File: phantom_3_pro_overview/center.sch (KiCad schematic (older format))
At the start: 3 parts

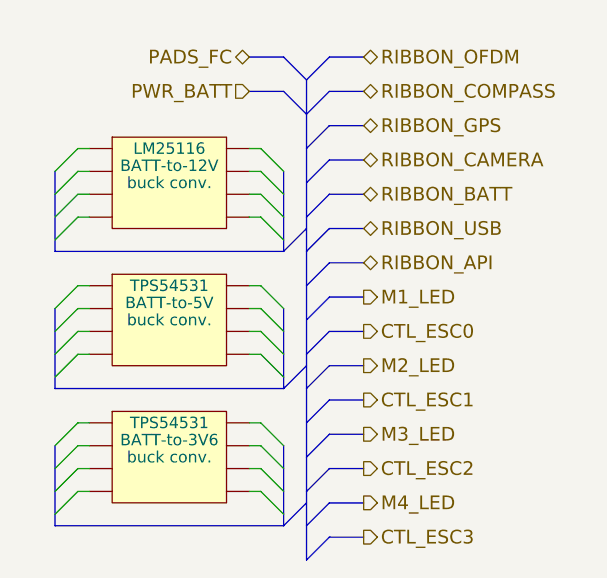
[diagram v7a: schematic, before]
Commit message: Overview: Separated gimbal power circuit.
This is to make sure the connection won't be interpreted as data link.
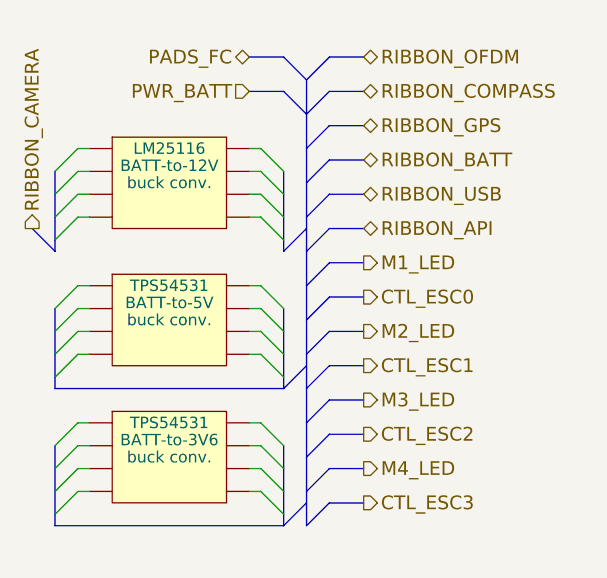
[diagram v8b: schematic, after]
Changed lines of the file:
@@
 $Descr User 5354 4725
 encoding utf-8
-Sheet 4 23
+Sheet 4 24
 Title "Overview of the Phantom 3 Pro Center part of MB"
 Date ""
@@
 Text HLabel 2950 1000 2    60   BiDi ~ 0
 RIBBON_GPS
+Text HLabel 1500 1450 1    60   Output ~ 0
+RIBBON_CAMERA
 Text HLabel 2950 1150 2    60   BiDi ~ 0
-RIBBON_CAMERA
+RIBBON_BATT
 Text HLabel 2950 1300 2    60   BiDi ~ 0
-RIBBON_BATT
+RIBBON_USB
 Text HLabel 2950 1450 2    60   BiDi ~ 0
-RIBBON_USB
-Text HLabel 2950 1600 2    60   BiDi ~ 0
 RIBBON_API
+Text HLabel 2950 1600 2    60   Output ~ 0
+M1_LED
 Text HLabel 2950 1750 2    60   Output ~ 0
-M1_LED
-Text HLabel 2950 1900 2    60   Output ~ 0
 CTL_ESC0
 Text HLabel 2450 850  0    60   Input ~ 0
 PWR_BATT
+Text HLabel 2950 1900 2    60   Output ~ 0
+M2_LED
 Text HLabel 2950 2050 2    60   Output ~ 0
-M2_LED
+CTL_ESC1
 Text HLabel 2950 2200 2    60   Output ~ 0
-CTL_ESC1
+M3_LED
 Text HLabel 2950 2350 2    60   Output ~ 0
-M3_LED
+CTL_ESC2
 Text HLabel 2950 2500 2    60   Output ~ 0
-CTL_ESC2
+M4_LED
 Text HLabel 2950 2650 2    60   Output ~ 0
-M4_LED
-Text HLabel 2950 2800 2    60   Output ~ 0
 CTL_ESC3
 Entry Bus Bus
@@
 Entry Bus Bus
 	2700 1100 2800 1000
+Wire Bus Line
+	2800 1000 2950 1000
 Entry Bus Bus
 	2700 1250 2800 1150
-Wire Bus Line
-	2800 1000 2950 1000
+Entry Bus Bus
+	2700 1400 2800 1300
 Wire Bus Line
 	2800 1150 2950 1150
-Entry Bus Bus
-	2700 1400 2800 1300
+Wire Bus Line
+	2800 1300 2950 1300
 Entry Bus Bus
 	2700 1550 2800 1450
-Wire Bus Line
-	2800 1300 2950 1300
+Entry Bus Bus
+	2700 1700 2800 1600
 Wire Bus Line
 	2800 1450 2950 1450
-Entry Bus Bus
-	2700 1700 2800 1600
+Wire Bus Line
+	2800 1600 2950 1600
 Entry Bus Bus
 	2700 1850 2800 1750
-Wire Bus Line
-	2800 1600 2950 1600
+Entry Bus Bus
+	2700 2000 2800 1900
 Wire Bus Line
 	2800 1750 2950 1750
-Entry Bus Bus
-	2700 2000 2800 1900
+Wire Bus Line
+	2800 1900 2950 1900
 Entry Bus Bus
 	2700 2150 2800 2050
-Wire Bus Line
-	2800 1900 2950 1900
+Entry Bus Bus
+	2700 2300 2800 2200
 Wire Bus Line
 	2800 2050 2950 2050
-Entry Bus Bus
-	2700 2300 2800 2200
+Wire Bus Line
+	2800 2200 2950 2200
 Entry Bus Bus
 	2700 2450 2800 2350
-Wire Bus Line
-	2800 2200 2950 2200
+Entry Bus Bus
+	2700 2600 2800 2500
 Wire Bus Line
 	2800 2350 2950 2350
-Entry Bus Bus
-	2700 2600 2800 2500
+Wire Bus Line
+	2800 2500 2950 2500
 Entry Bus Bus
 	2700 2750 2800 2650
 Wire Bus Line
-	2800 2500 2950 2500
-Wire Bus Line
 	2800 2650 2950 2650
-Entry Bus Bus
-	2700 2900 2800 2800
-Wire Bus Line
-	2800 2800 2950 2800
 Entry Wire Line
 	2500 1100 2600 1200
@@
 	2500 2000 2600 2100
 Entry Wire Line
-	2500 2300 2600 2400
-Entry Wire Line
-	2500 2400 2600 2500
-Entry Wire Line
-	2500 2500 2600 2600
-Entry Wire Line
-	2500 2600 2600 2700
-Entry Wire Line
 	1600 1200 1700 1100
 Entry Wire Line
@@
 Entry Wire Line
 	1600 2100 1700 2000
-Entry Wire Line
-	1600 2400 1700 2300
-Entry Wire Line
-	1600 2500 1700 2400
-Entry Wire Line
-	1600 2600 1700 2500
-Entry Wire Line
-	1600 2700 1700 2600
-Wire Bus Line
-	1600 1200 1600 1550
-Wire Bus Line
-	2600 1200 2600 1550
-Wire Bus Line
-	1600 1800 1600 2150
-Wire Bus Line
-	2600 2150 1600 2150
-Wire Bus Line
-	2600 1800 2600 2150
-Wire Bus Line
-	1600 2400 1600 2750
-Wire Bus Line
-	2600 2750 1600 2750
-Wire Bus Line
-	2600 2400 2600 2750
+Wire Bus Line
+	1600 1200 1600 1300
+Wire Bus Line
+	1600 1300 1600 1400
+Wire Bus Line
+	1600 1400 1600 1500
+Wire Bus Line
+	1600 1500 1600 1550
+Wire Bus Line
+	2600 1200 2600 1300
+Wire Bus Line
+	2600 1300 2600 1400
+Wire Bus Line
+	2600 1400 2600 1500
+Wire Bus Line
+	2600 1500 2600 1550
+Wire Bus Line
+	1600 1800 1600 1900
+Wire Bus Line
+	1600 1900 1600 2000
+Wire Bus Line
+	1600 2000 1600 2100
+Wire Bus Line
+	1600 2100 1600 2150
+Wire Bus Line
+	1600 2150 2600 2150
+Wire Bus Line
+	2600 2150 2600 2100
+Wire Bus Line
+	2600 2100 2600 2000
+Wire Bus Line
+	2600 2000 2600 1900
+Wire Bus Line
+	2600 1900 2600 1800
 Entry Bus Bus
 	2600 1550 2700 1450
 Entry Bus Bus
 	2600 2150 2700 2050
-Entry Bus Bus
-	2600 2750 2700 2650
-$Comp
-L IC_DIL8 U?
-U 1 1 5992D357
-P 2100 2450
-F 0 "U?" H 2100 2300 50  0001 C CNN
-F 1 "TPS54531" H 2100 2600 50  0000 C CNN
-F 2 "BATT-to-3V6" H 2100 2525 50  0000 C CNN
-F 3 "buck conv." H 2100 2450 50  0000 C CNN
-	1    2100 2450
-	1    0    0    -1
-$EndComp
 $Comp
 L IC_DIL8 U?
@@
 	1    0    0    -1
 $EndComp
-Wire Bus Line
-	2600 1550 1600 1550
+Wire Wire Line
+	2450 2000 2500 2000
+Wire Wire Line
+	2500 1900 2450 1900
+Wire Wire Line
+	2450 1800 2500 1800
+Wire Wire Line
+	2500 1700 2450 1700
+Wire Wire Line
+	1750 1700 1700 1700
+Wire Wire Line
+	1700 1800 1750 1800
+Wire Wire Line
+	1750 1900 1700 1900
+Wire Wire Line
+	1700 2000 1750 2000
+Wire Wire Line
+	1700 1400 1750 1400
+Wire Wire Line
+	1700 1300 1750 1300
+Wire Wire Line
+	1750 1200 1700 1200
+Wire Wire Line
+	1700 1100 1750 1100
+Wire Wire Line
+	2450 1100 2500 1100
+Wire Wire Line
+	2500 1200 2450 1200
+Wire Wire Line
+	2450 1300 2500 1300
+Wire Wire Line
+	2500 1400 2450 1400
+Wire Bus Line
+	2700 800  2700 950
+Wire Bus Line
+	2700 950  2700 1100
+Wire Bus Line
+	2700 1100 2700 1250
+Wire Bus Line
+	2700 1250 2700 1400
+Wire Bus Line
+	2700 1400 2700 1450
+Wire Bus Line
+	2700 1450 2700 1550
+Wire Bus Line
+	2700 1550 2700 1700
+Wire Bus Line
+	2700 1700 2700 1850
+Wire Bus Line
+	2700 1850 2700 2000
+Wire Bus Line
+	2700 2000 2700 2050
+Wire Bus Line
+	2700 2050 2700 2150
+Wire Bus Line
+	2700 2150 2700 2300
+Wire Bus Line
+	2700 2300 2700 2450
+Wire Bus Line
+	2700 2450 2700 2600
+Wire Bus Line
+	2700 2600 2700 2650
+Wire Bus Line
+	2700 2650 2700 2750
+Wire Bus Line
+	2700 2750 2700 2750
+Wire Bus Line
+	1600 1550 1500 1450
+Wire Wire Line
+	2500 2300 2450 2300
+Wire Wire Line
+	2450 2400 2500 2400
+Wire Wire Line
+	2500 2500 2450 2500
+Wire Wire Line
+	2450 2600 2500 2600
+Wire Wire Line
+	1750 2600 1700 2600
+Wire Wire Line
+	1700 2500 1750 2500
+Wire Wire Line
+	1750 2400 1700 2400
 Wire Wire Line
 	1700 2300 1750 2300
-Wire Wire Line
-	1750 2400 1700 2400
-Wire Wire Line
-	1700 2500 1750 2500
-Wire Wire Line
-	1750 2600 1700 2600
-Wire Wire Line
-	2450 2600 2500 2600
-Wire Wire Line
-	2500 2500 2450 2500
-Wire Wire Line
-	2450 2400 2500 2400
-Wire Wire Line
-	2500 2300 2450 2300
-Wire Wire Line
-	2450 2000 2500 2000
-Wire Wire Line
-	2500 1900 2450 1900
-Wire Wire Line
-	2450 1800 2500 1800
-Wire Wire Line
-	2500 1700 2450 1700
-Wire Wire Line
-	1750 1700 1700 1700
-Wire Wire Line
-	1700 1800 1750 1800
-Wire Wire Line
-	1750 1900 1700 1900
-Wire Wire Line
-	1700 2000 1750 2000
-Wire Wire Line
-	1700 1400 1750 1400
-Wire Wire Line
-	1700 1300 1750 1300
-Wire Wire Line
-	1750 1200 1700 1200
-Wire Wire Line
-	1700 1100 1750 1100
-Wire Wire Line
-	2450 1100 2500 1100
-Wire Wire Line
-	2500 1200 2450 1200
-Wire Wire Line
-	2450 1300 2500 1300
-Wire Wire Line
-	2500 1400 2450 1400
-Wire Bus Line
-	2700 800  2700 2900
+$Comp
+L IC_DIL8 U?
+U 1 1 5992D357
+P 2100 2450
+F 0 "U?" H 2100 2300 50  0001 C CNN
+F 1 "TPS54531" H 2100 2600 50  0000 C CNN
+F 2 "BATT-to-3V6" H 2100 2525 50  0000 C CNN
+F 3 "buck conv." H 2100 2450 50  0000 C CNN
+	1    2100 2450
+	1    0    0    -1
+$EndComp
+Entry Bus Bus
+	2600 2750 2700 2650
+Wire Bus Line
+	2600 2500 2600 2400
+Wire Bus Line
+	2600 2600 2600 2500
+Wire Bus Line
+	2600 2700 2600 2600
+Wire Bus Line
+	2600 2750 2600 2700
+Wire Bus Line
+	1600 2750 2600 2750
+Wire Bus Line
+	1600 2700 1600 2750
+Wire Bus Line
+	1600 2600 1600 2700
+Wire Bus Line
+	1600 2500 1600 2600
+Wire Bus Line
+	1600 2400 1600 2500
+Entry Wire Line
+	1600 2700 1700 2600
+Entry Wire Line
+	1600 2600 1700 2500
+Entry Wire Line
+	1600 2500 1700 2400
+Entry Wire Line
+	1600 2400 1700 2300
+Entry Wire Line
+	2500 2600 2600 2700
+Entry Wire Line
+	2500 2500 2600 2600
+Entry Wire Line
+	2500 2400 2600 2500
+Entry Wire Line
+	2500 2300 2600 2400
 $EndSCHEMATC
